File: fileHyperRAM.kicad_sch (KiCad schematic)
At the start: 15 parts, among them U4 S70KS1281

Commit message: Fix some checker complaints
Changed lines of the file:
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@@
     (pin "E5")
   )
+  (symbol (lib_id "power:PWR_FLAG") (at 123.19 50.8 0) (unit 1)
+    (in_bom yes) (on_board yes)
+    (property "Reference" "#FLG0107" (id 0) (at 123.19 48.895 0)
+      (effects (font (size 1.27 1.27)) hide)
+    )
+    (property "Value" "PWR_FLAG" (id 1) (at 123.19 46.4058 0))
+    (property "Footprint" "" (id 2) (at 123.19 50.8 0)
+      (effects (font (size 1.27 1.27)) hide)
+    )
+    (property "Datasheet" "~" (id 3) (at 123.19 50.8 0)
+      (effects (font (size 1.27 1.27)) hide)
+    )
+    (pin "1")
+  )
+  (symbol (lib_id "power:PWR_FLAG") (at 123.19 77.47 0) (unit 1)
+    (in_bom yes) (on_board yes)
+    (property "Reference" "#FLG0106" (id 0) (at 123.19 75.565 0)
+      (effects (font (size 1.27 1.27)) hide)
+    )
+    (property "Value" "PWR_FLAG" (id 1) (at 123.19 73.0758 0))
+    (property "Footprint" "" (id 2) (at 123.19 77.47 0)
+      (effects (font (size 1.27 1.27)) hide)
+    )
+    (property "Datasheet" "~" (id 3) (at 123.19 77.47 0)
+      (effects (font (size 1.27 1.27)) hide)
+    )
+    (pin "1")
+  )
 )

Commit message: Update Mouser prices
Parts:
- C21, C22, C34, C35, C36, C37: Pricing (EUR) 0,09 -> 0,10
- C30, C31, C32, C33: Pricing (EUR) 0,09 -> 0,02
- FB2, FB3: Pricing (EUR) 0,09 -> 0,12
- U4: Pricing (EUR) 7,00 -> 7,31
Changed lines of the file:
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@@
       (effects (font (size 1.27 1.27)) hide)
     )
-    (property "Pricing (EUR)" "0,09" (id 7) (at 82.55 50.8 0)
+    (property "Pricing (EUR)" "0,10" (id 7) (at 82.55 50.8 0)
       (effects (font (size 1.27 1.27)) hide)
     )
@@
       (effects (font (size 1.27 1.27)) hide)
     )
-    (property "Pricing (EUR)" "0,09" (id 7) (at 87.63 50.8 0)
+    (property "Pricing (EUR)" "0,10" (id 7) (at 87.63 50.8 0)
       (effects (font (size 1.27 1.27)) hide)
     )
@@
       (effects (font (size 1.27 1.27)) hide)
     )
-    (property "Pricing (EUR)" "0,09" (id 7) (at 59.69 50.8 0)
+    (property "Pricing (EUR)" "0,02" (id 7) (at 59.69 50.8 0)
       (effects (font (size 1.27 1.27)) hide)
     )
@@
       (effects (font (size 1.27 1.27)) hide)
     )
-    (property "Pricing (EUR)" "0,09" (id 7) (at 64.77 50.8 0)
+    (property "Pricing (EUR)" "0,02" (id 7) (at 64.77 50.8 0)
       (effects (font (size 1.27 1.27)) hide)
     )
@@
       (effects (font (size 1.27 1.27)) hide)
     )
-    (property "Pricing (EUR)" "0,09" (id 7) (at 82.55 31.75 0)
+    (property "Pricing (EUR)" "0,10" (id 7) (at 82.55 31.75 0)
       (effects (font (size 1.27 1.27)) hide)
     )
@@
       (effects (font (size 1.27 1.27)) hide)
     )
-    (property "Pricing (EUR)" "0,09" (id 7) (at 87.63 31.75 0)
+    (property "Pricing (EUR)" "0,10" (id 7) (at 87.63 31.75 0)
       (effects (font (size 1.27 1.27)) hide)
     )
@@
       (effects (font (size 1.27 1.27)) hide)
     )
-    (property "Pricing (EUR)" "0,09" (id 7) (at 59.69 31.75 0)
+    (property "Pricing (EUR)" "0,02" (id 7) (at 59.69 31.75 0)
       (effects (font (size 1.27 1.27)) hide)
     )
@@
       (effects (font (size 1.27 1.27)) hide)
     )
-    (property "Pricing (EUR)" "0,09" (id 7) (at 64.77 31.75 0)
+    (property "Pricing (EUR)" "0,02" (id 7) (at 64.77 31.75 0)
       (effects (font (size 1.27 1.27)) hide)
     )
@@
       (effects (font (size 1.27 1.27)) hide)
     )
-    (property "Pricing (EUR)" "0,09" (id 7) (at 123.19 57.15 0)
+    (property "Pricing (EUR)" "0,10" (id 7) (at 123.19 57.15 0)
       (effects (font (size 1.27 1.27)) hide)
     )
@@
       (effects (font (size 1.27 1.27)) hide)
     )
-    (property "Pricing (EUR)" "0,09" (id 7) (at 133.35 50.8 0)
+    (property "Pricing (EUR)" "0,12" (id 7) (at 133.35 50.8 0)
       (effects (font (size 1.27 1.27)) hide)
     )
@@
       (effects (font (size 1.27 1.27)) hide)
     )
-    (property "Pricing (EUR)" "0,09" (id 7) (at 123.19 83.82 0)
+    (property "Pricing (EUR)" "0,10" (id 7) (at 123.19 83.82 0)
       (effects (font (size 1.27 1.27)) hide)
     )
@@
       (effects (font (size 1.27 1.27)) hide)
     )
-    (property "Pricing (EUR)" "0,09" (id 7) (at 133.35 77.47 0)
+    (property "Pricing (EUR)" "0,12" (id 7) (at 133.35 77.47 0)
       (effects (font (size 1.27 1.27)) hide)
     )
@@
       (effects (font (size 1.27 1.27)) hide)
     )
-    (property "Pricing (EUR)" "7,00" (id 7) (at 58.42 74.93 0)
-      (effects (font (size 1.27 1.27)) hide)
-    )
+    (property "Pricing (EUR)" "7,31" (id 7) (at 58.42 74.93 0)
+      (effects (font (size 1.27 1.27)) hide)
+    )

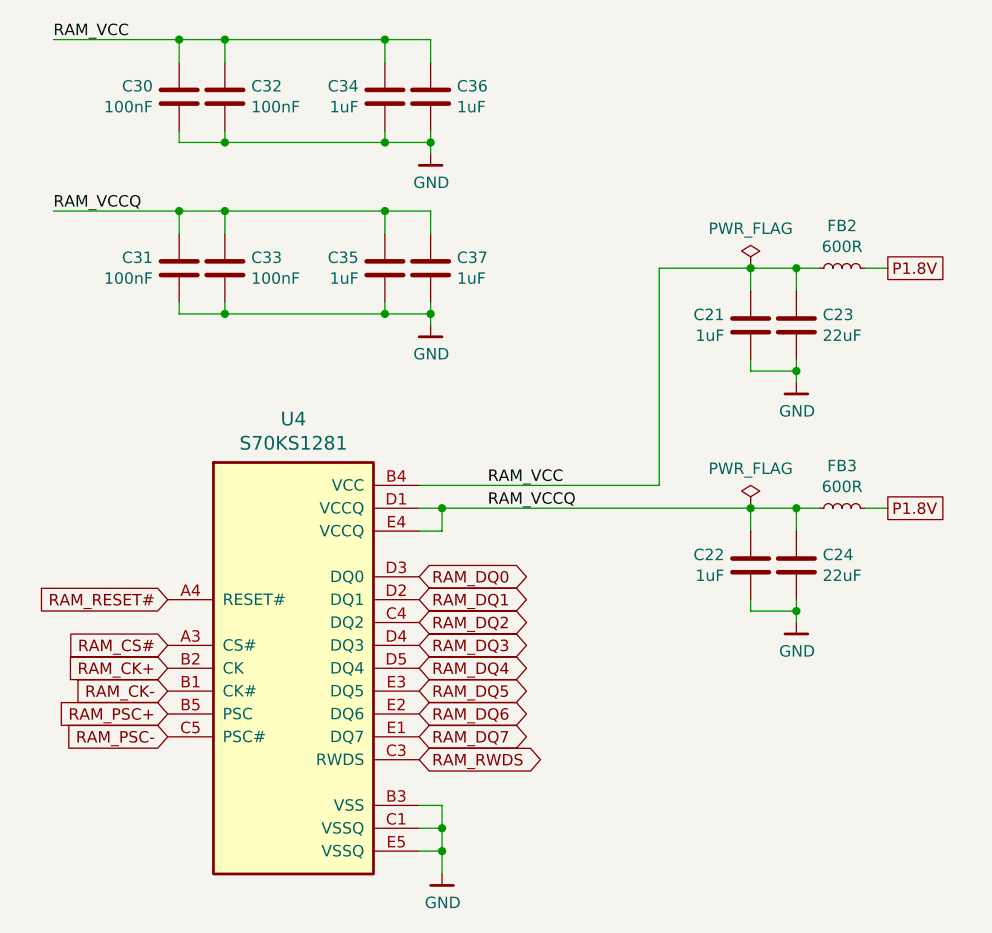
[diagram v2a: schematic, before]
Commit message: Replace HyperRAM with 3V Winbond part
Also remove PSC/PSC# as they are not used on 3V parts.
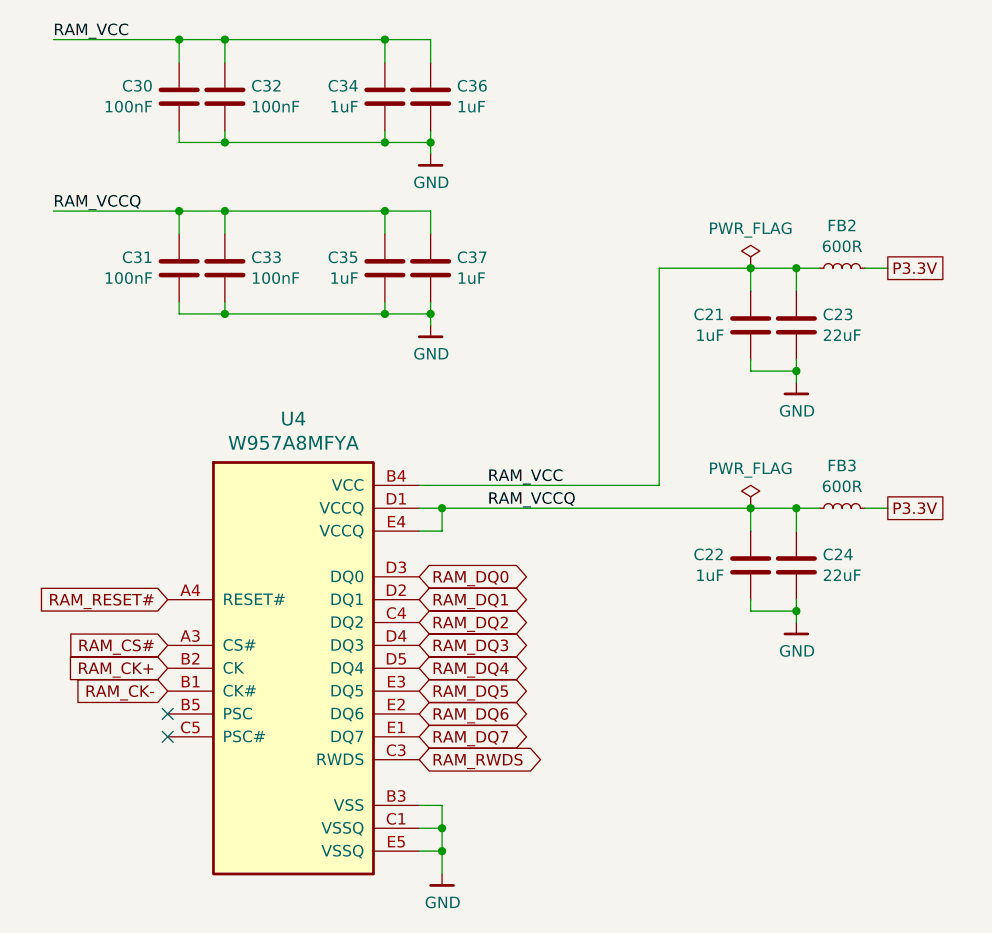
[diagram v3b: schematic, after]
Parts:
- U4: value S70KS1281 -> W957A8MFYA; Mfg Cypress Semiconductor -> Winbond; Mouser Part No 727-S70KS1281DPBHI02 -> 454-W957A8MFYA5I; PN S70KS1281DPBHI020 -> W957A8MFYA5I; Pricing (EUR) 7,31 -> 4,19
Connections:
- net P1.8V renamed P3.3V
- net RAM_PSC+: no longer names the net of U4.B5 (PSC)
- net RAM_PSC-: no longer names the net of U4.C5 (PSC#)
- no-connect marks 0 -> 2
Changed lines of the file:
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@@
   (junction (at 64.77 55.88) (diameter 0) (color 0 0 0 0)
   )
+  (no_connect (at 58.42 100.33))
+  (no_connect (at 58.42 102.87))
   (wire (pts (xy 88.9 80.01) (xy 88.9 77.47))
     (stroke (width 0) (type default) (color 0 0 0 0))
@@
     )
   )
-  (global_label "P1.8V" (shape passive) (at 138.43 50.8 0) (fields_autoplaced)
-    (effects (font (size 1.27 1.27)) (justify left))
-    (property "Intersheet References" "${INTERSHEET_REFS}" (id 0) (at 0 0 0)
+  (global_label "P3.3V" (shape passive) (at 138.43 77.47 0) (fields_autoplaced)
+    (effects (font (size 1.27 1.27)) (justify left))
+    (property "Intersheet References" "${INTERSHEET_REFS}" (id 0) (at -133.35 -59.69 0)
       (effects (font (size 1.27 1.27)) hide)
     )
@@
     )
   )
-  (global_label "RAM_PSC+" (shape input) (at 58.42 100.33 180) (fields_autoplaced)
-    (effects (font (size 1.27 1.27)) (justify right))
-    (property "Intersheet References" "${INTERSHEET_REFS}" (id 0) (at 0 0 0)
-      (effects (font (size 1.27 1.27)) hide)
-    )
-  )
   (global_label "RAM_RESET#" (shape input) (at 58.42 87.63 180) (fields_autoplaced)
     (effects (font (size 1.27 1.27)) (justify right))
@@
     )
   )
+  (global_label "P3.3V" (shape passive) (at 138.43 50.8 0) (fields_autoplaced)
+    (effects (font (size 1.27 1.27)) (justify left))
+    (property "Intersheet References" "${INTERSHEET_REFS}" (id 0) (at -133.35 -86.36 0)
+      (effects (font (size 1.27 1.27)) hide)
+    )
+  )
   (global_label "RAM_DQ1" (shape bidirectional) (at 86.36 87.63 0) (fields_autoplaced)
     (effects (font (size 1.27 1.27)) (justify left))
-    (property "Intersheet References" "${INTERSHEET_REFS}" (id 0) (at 0 0 0)
-      (effects (font (size 1.27 1.27)) hide)
-    )
-  )
-  (global_label "P1.8V" (shape passive) (at 138.43 77.47 0) (fields_autoplaced)
-    (effects (font (size 1.27 1.27)) (justify left))
-    (property "Intersheet References" "${INTERSHEET_REFS}" (id 0) (at 0 0 0)
-      (effects (font (size 1.27 1.27)) hide)
-    )
-  )
-  (global_label "RAM_PSC-" (shape input) (at 58.42 102.87 180) (fields_autoplaced)
-    (effects (font (size 1.27 1.27)) (justify right))
     (property "Intersheet References" "${INTERSHEET_REFS}" (id 0) (at 0 0 0)
       (effects (font (size 1.27 1.27)) hide)
@@
       (effects (font (size 1.524 1.524)))
     )
-    (property "Value" "S70KS1281" (id 1) (at 72.39 70.2564 0)
+    (property "Value" "W957A8MFYA" (id 1) (at 72.39 70.2564 0)
       (effects (font (size 1.524 1.524)))
     )
@@
       (effects (font (size 1.27 1.27)) hide)
     )
-    (property "Mfg" "Cypress Semiconductor" (id 4) (at 58.42 74.93 0)
-      (effects (font (size 1.27 1.27)) hide)
-    )
-    (property "Mouser Part No" "727-S70KS1281DPBHI02" (id 5) (at 58.42 74.93 0)
-      (effects (font (size 1.27 1.27)) hide)
-    )
-    (property "PN" "S70KS1281DPBHI020" (id 6) (at 58.42 74.93 0)
-      (effects (font (size 1.27 1.27)) hide)
-    )
-    (property "Pricing (EUR)" "7,31" (id 7) (at 58.42 74.93 0)
-      (effects (font (size 1.27 1.27)) hide)
-    )
+    (property "Mfg" "Winbond" (id 4) (at 58.42 74.93 0)
+      (effects (font (size 1.27 1.27)) hide)
+    )
+    (property "Mouser Part No" "454-W957A8MFYA5I" (id 5) (at 58.42 74.93 0)
+      (effects (font (size 1.27 1.27)) hide)
+    )
+    (property "PN" "W957A8MFYA5I" (id 6) (at 58.42 74.93 0)
+      (effects (font (size 1.27 1.27)) hide)
+    )
+    (property "Pricing (EUR)" "4,19" (id 7) (at 58.42 74.93 0)
+      (effects (font (size 1.27 1.27)) hide)
+    )
